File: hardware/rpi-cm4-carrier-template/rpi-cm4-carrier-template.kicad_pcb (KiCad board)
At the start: 2 copper layers, 21.8 x 55 mm, 10 parts, among them J1 USB4110-GF-A_REVB, U1 NLV17SZ07DFT2G

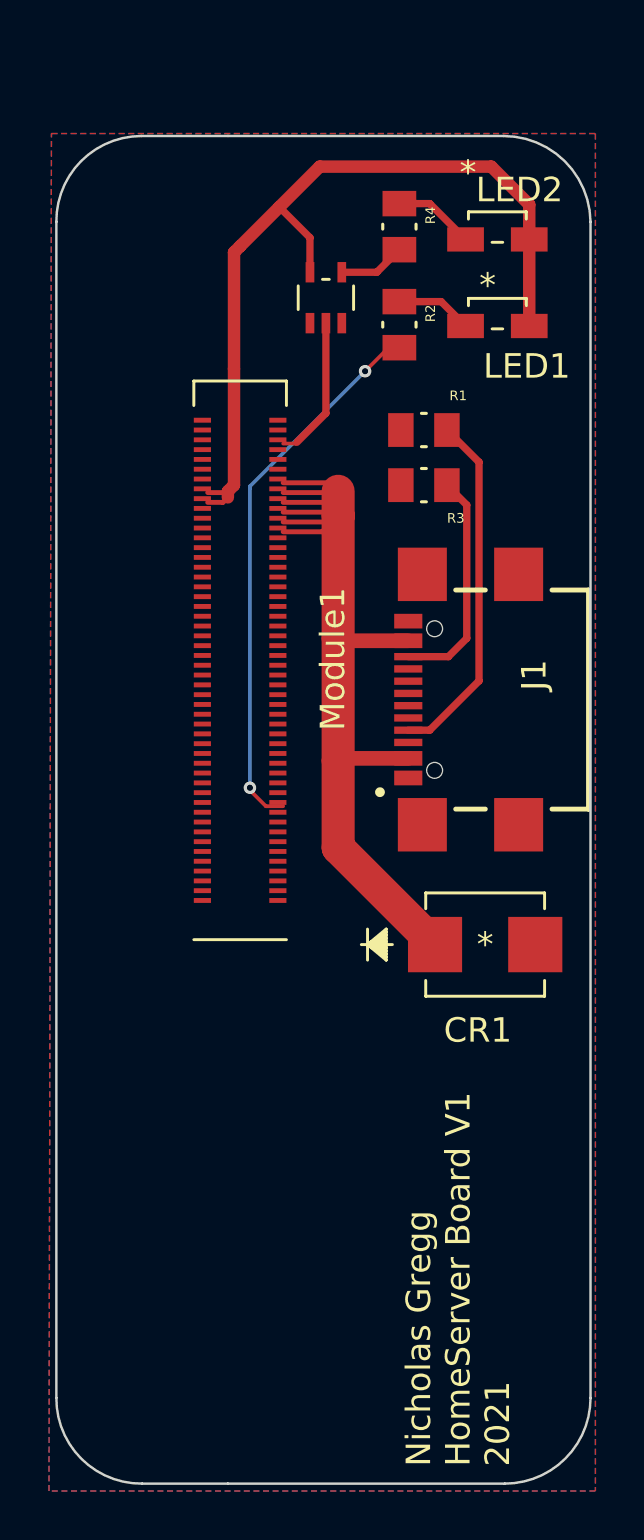
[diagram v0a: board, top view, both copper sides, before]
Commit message: updated PCB layout
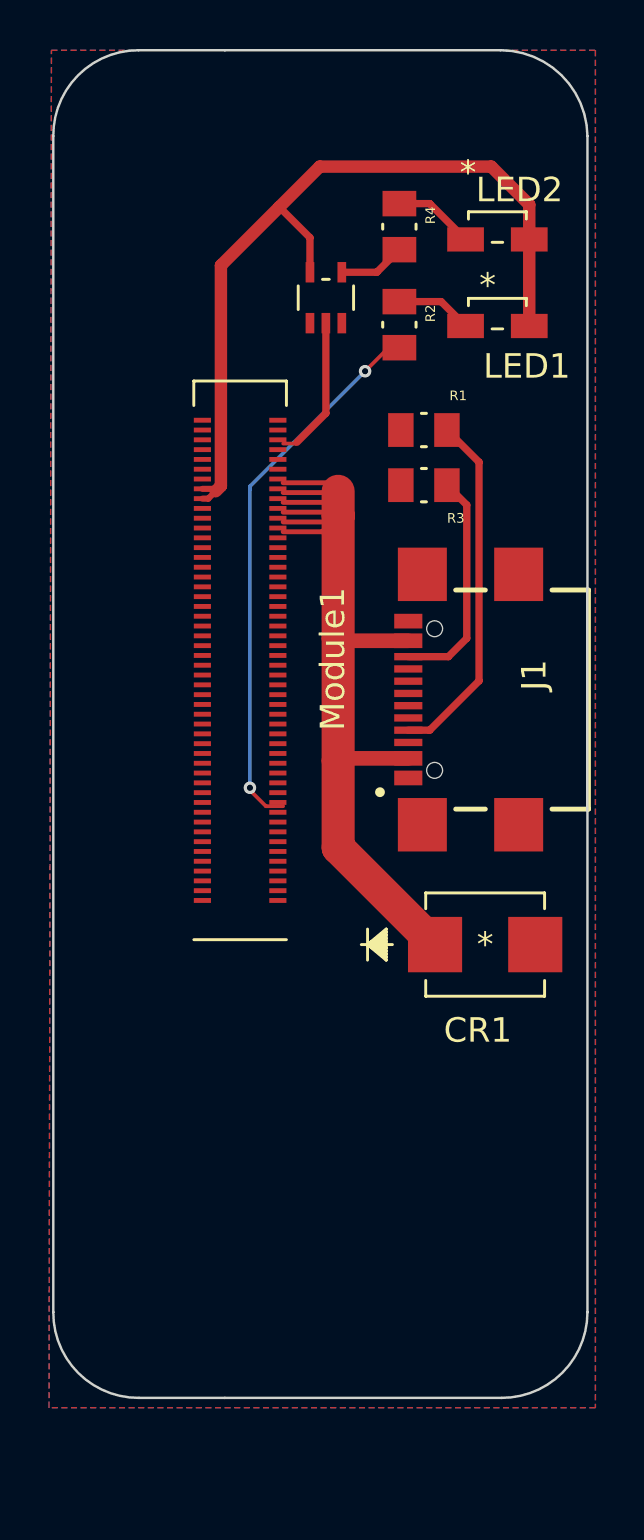
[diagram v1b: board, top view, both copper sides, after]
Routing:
- net +3.3V: track 34.1 -> 33.6 mm
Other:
- board text removed: "Nicholas Gregg HomeServer Board V1 2021"
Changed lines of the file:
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@@
     )
     (pad_to_mask_clearance 0)
+    (grid_origin 163.5 100)
     (pcbplotparams
       (layerselection 0x00010fc_ffffffff)
       (disableapertmacros false)
-      (usegerberextensions true)
+      (usegerberextensions false)
       (usegerberattributes true)
       (usegerberadvancedattributes true)
@@
       (drillshape 0)
       (scaleselection 1)
-      (outputdirectory "C:/Users/nicho/Documents/git/HomeServer/Gerbers/")
+      (outputdirectory "../../Gerbers/")
     )
   )
@@
     )
   )
-  (gr_line (start 177.8 130) (end 177.8 82) (layer "Edge.Cuts") (width 0.1))
-  (gr_line (start 163 78.5) (end 174.25 78.5) (layer "Edge.Cuts") (width 0.1))
-  (gr_arc (start 156 82) (mid 157.008868 79.526661) (end 159.474874 78.5) (layer "Edge.Cuts") (width 0.1))
-  (gr_line (start 156 82) (end 156 130) (layer "Edge.Cuts") (width 0.1))
-  (gr_arc (start 159.5 133.499999) (mid 157.017782 132.482217) (end 156 130) (layer "Edge.Cuts") (width 0.1))
-  (gr_line (start 159.5 133.5) (end 163 133.5) (layer "Edge.Cuts") (width 0.1))
-  (gr_arc (start 177.8 130) (mid 176.774874 132.474874) (end 174.3 133.5) (layer "Edge.Cuts") (width 0.1))
-  (gr_arc (start 174.25 78.5) (mid 176.742614 79.522134) (end 177.8 82) (layer "Edge.Cuts") (width 0.1))
-  (gr_line (start 163 133.5) (end 174.3 133.5) (layer "Edge.Cuts") (width 0.1))
-  (gr_line (start 159.474874 78.5) (end 163 78.5) (layer "Edge.Cuts") (width 0.1))
-  (gr_text "Nicholas Gregg\nHomeServer Board V1\n2021" (at 172.4 132.8 90) (layer "F.SilkS")
-    (effects (font (size 1 1) (thickness 0.2)) (justify left))
-  )
+  (gr_line (start 177.675 126.5) (end 177.675 78.5) (layer "Edge.Cuts") (width 0.1))
+  (gr_line (start 162.875 75) (end 174.125 75) (layer "Edge.Cuts") (width 0.1))
+  (gr_arc (start 155.875 78.5) (mid 156.883868 76.026661) (end 159.349874 75) (layer "Edge.Cuts") (width 0.1))
+  (gr_line (start 155.875 78.5) (end 155.875 126.5) (layer "Edge.Cuts") (width 0.1))
+  (gr_arc (start 159.375 129.999999) (mid 156.892782 128.982217) (end 155.875 126.5) (layer "Edge.Cuts") (width 0.1))
+  (gr_line (start 159.375 130) (end 162.875 130) (layer "Edge.Cuts") (width 0.1))
+  (gr_arc (start 177.675 126.5) (mid 176.649874 128.974874) (end 174.175 130) (layer "Edge.Cuts") (width 0.1))
+  (gr_arc (start 174.125 75) (mid 176.617614 76.022134) (end 177.675 78.5) (layer "Edge.Cuts") (width 0.1))
+  (gr_line (start 162.875 130) (end 174.175 130) (layer "Edge.Cuts") (width 0.1))
+  (gr_line (start 159.349874 75) (end 162.875 75) (layer "Edge.Cuts") (width 0.1))
   (segment (start 167.047018 93.452982) (end 167.5 93) (width 0.2) (layer "F.Cu") (net 1))
   (segment (start 170.3625 103.9) (end 167.6 103.9) (width 0.6) (layer "F.Cu") (net 1))
@@
   (segment (start 171.7053 85.26) (end 172.7 86.2547) (width 0.3) (layer "F.Cu") (net 11))
   (segment (start 170 85.26) (end 171.7053 85.26) (width 0.3) (layer "F.Cu") (net 11))
-  (segment (start 163 93) (end 163 93.25) (width 0.508) (layer "F.Cu") (net 12))
+  (segment (start 165.1 81.4) (end 162.715911 83.784089) (width 0.508) (layer "F.Cu") (net 12))
+  (segment (start 162.2 93.3) (end 162.5 93) (width 0.25) (layer "F.Cu") (net 12))
+  (segment (start 161.96 92.9) (end 162.4 92.9) (width 0.25) (layer "F.Cu") (net 12))
   (segment (start 166.75 79.75) (end 173.75 79.75) (width 0.508) (layer "F.Cu") (net 12))
   (segment (start 166.350001 84.061051) (end 166.350001 82.650001) (width 0.3) (layer "F.Cu") (net 12))
   (segment (start 173.75 79.75) (end 175.3 81.3) (width 0.508) (layer "F.Cu") (net 12))
   (segment (start 175.3 81.3) (end 175.3 82.7215) (width 0.508) (layer "F.Cu") (net 12))
-  (segment (start 162.947018 93.052982) (end 163 93) (width 0.2) (layer "F.Cu") (net 12))
-  (segment (start 162.176655 93.052982) (end 162.947018 93.052982) (width 0.2) (layer "F.Cu") (net 12))
-  (segment (start 162.176655 93.452982) (end 162.797018 93.452982) (width 0.2) (layer "F.Cu") (net 12))
+  (segment (start 161.96 93.3) (end 162.2 93.3) (width 0.25) (layer "F.Cu") (net 12))
+  (segment (start 162.715911 83.784089) (end 162.715911 92.784089) (width 0.508) (layer "F.Cu") (net 12))
   (segment (start 165.1 81.4) (end 166.75 79.75) (width 0.508) (layer "F.Cu") (net 12))
-  (segment (start 162.797018 93.452982) (end 163 93.25) (width 0.2) (layer "F.Cu") (net 12))
-  (segment (start 163.5 83) (end 163.25 83.25) (width 0.508) (layer "F.Cu") (net 12))
+  (segment (start 162.4 92.9) (end 162.5 93) (width 0.25) (layer "F.Cu") (net 12))
   (segment (start 166.350001 82.650001) (end 165.1 81.4) (width 0.3) (layer "F.Cu") (net 12))
-  (segment (start 165.1 81.4) (end 163.5 83) (width 0.508) (layer "F.Cu") (net 12))
+  (segment (start 162.715911 92.784089) (end 162.5 93) (width 0.508) (layer "F.Cu") (net 12))
   (segment (start 175.3 86.2547) (end 175.3 82.7215) (width 0.508) (layer "F.Cu") (net 12))
-  (segment (start 163.25 92.75) (end 163 93) (width 0.508) (layer "F.Cu") (net 12))
-  (segment (start 163.25 88) (end 163.25 92.75) (width 0.508) (layer "F.Cu") (net 12))
-  (segment (start 163.25 83.25) (end 163.25 88) (width 0.508) (layer "F.Cu") (net 12))
   (segment (start 171.2385 81.26) (end 172.7 82.7215) (width 0.3) (layer "F.Cu") (net 13))
   (segment (start 170 81.26) (end 171.2385 81.26) (width 0.3) (layer "F.Cu") (net 13))
@@
     (polygon
       (pts
-        (xy 178 133.8)
-        (xy 155.7 133.8)
-        (xy 155.8 78.4)
-        (xy 178 78.4)
+        (xy 178 130.4)
+        (xy 155.7 130.4)
+        (xy 155.8 75)
+        (xy 178 75)
       )
     )
